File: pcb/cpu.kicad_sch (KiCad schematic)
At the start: 12 parts, among them J9 x2 Multiplier, U1 486Socket

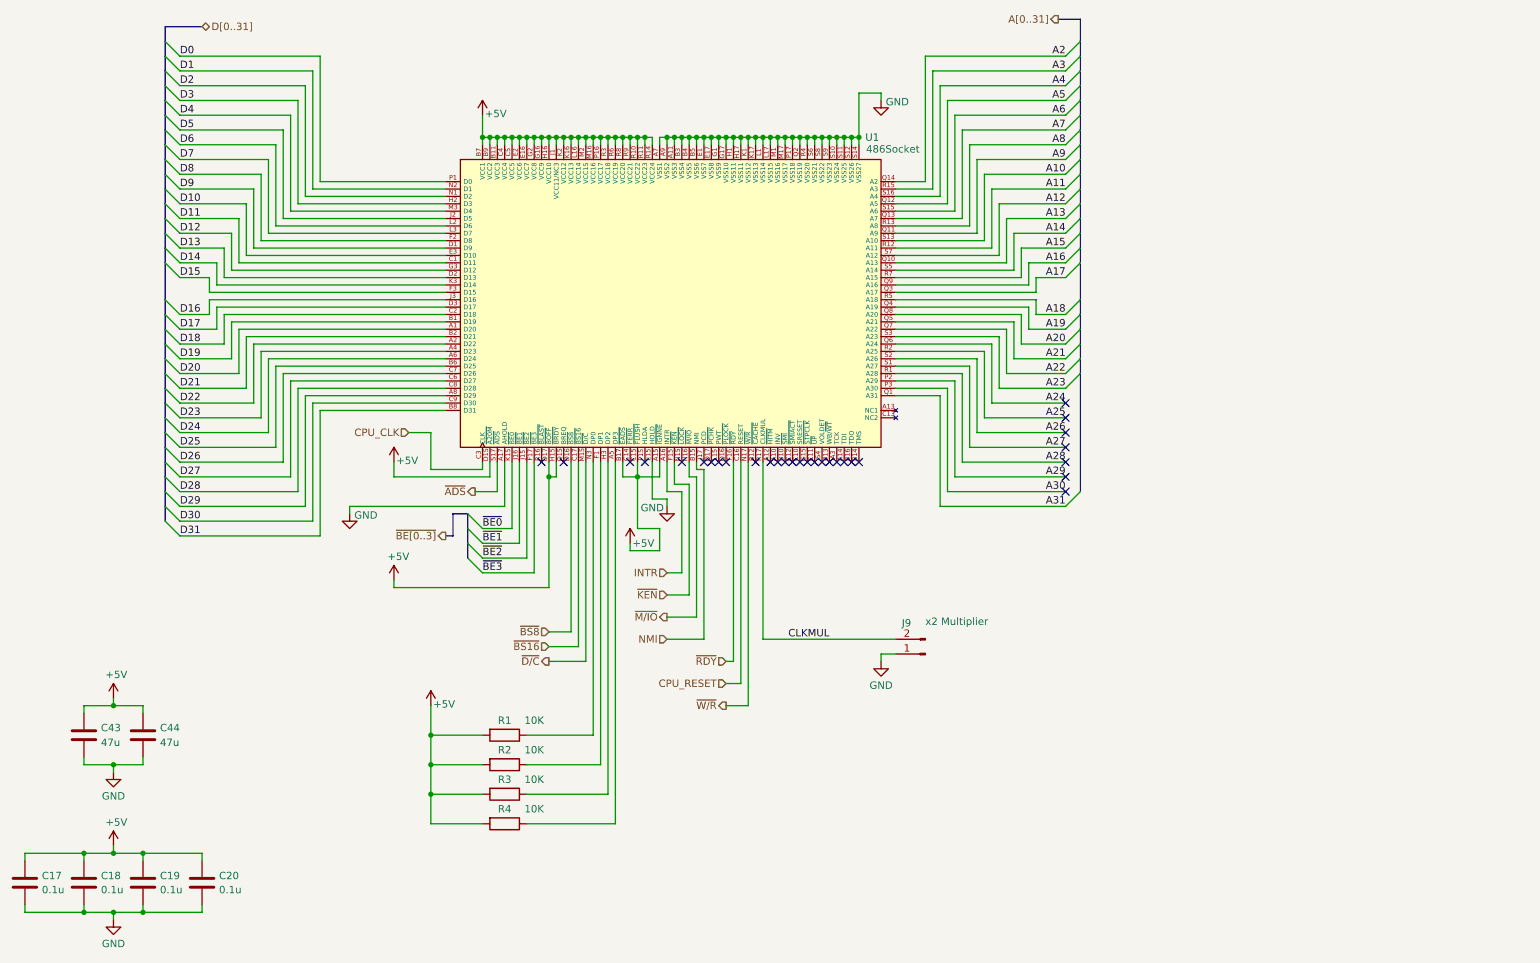
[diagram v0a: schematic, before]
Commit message: CPU diagram DMA/Burst pins pulled out to test points near FPGA IO ready for experimentation
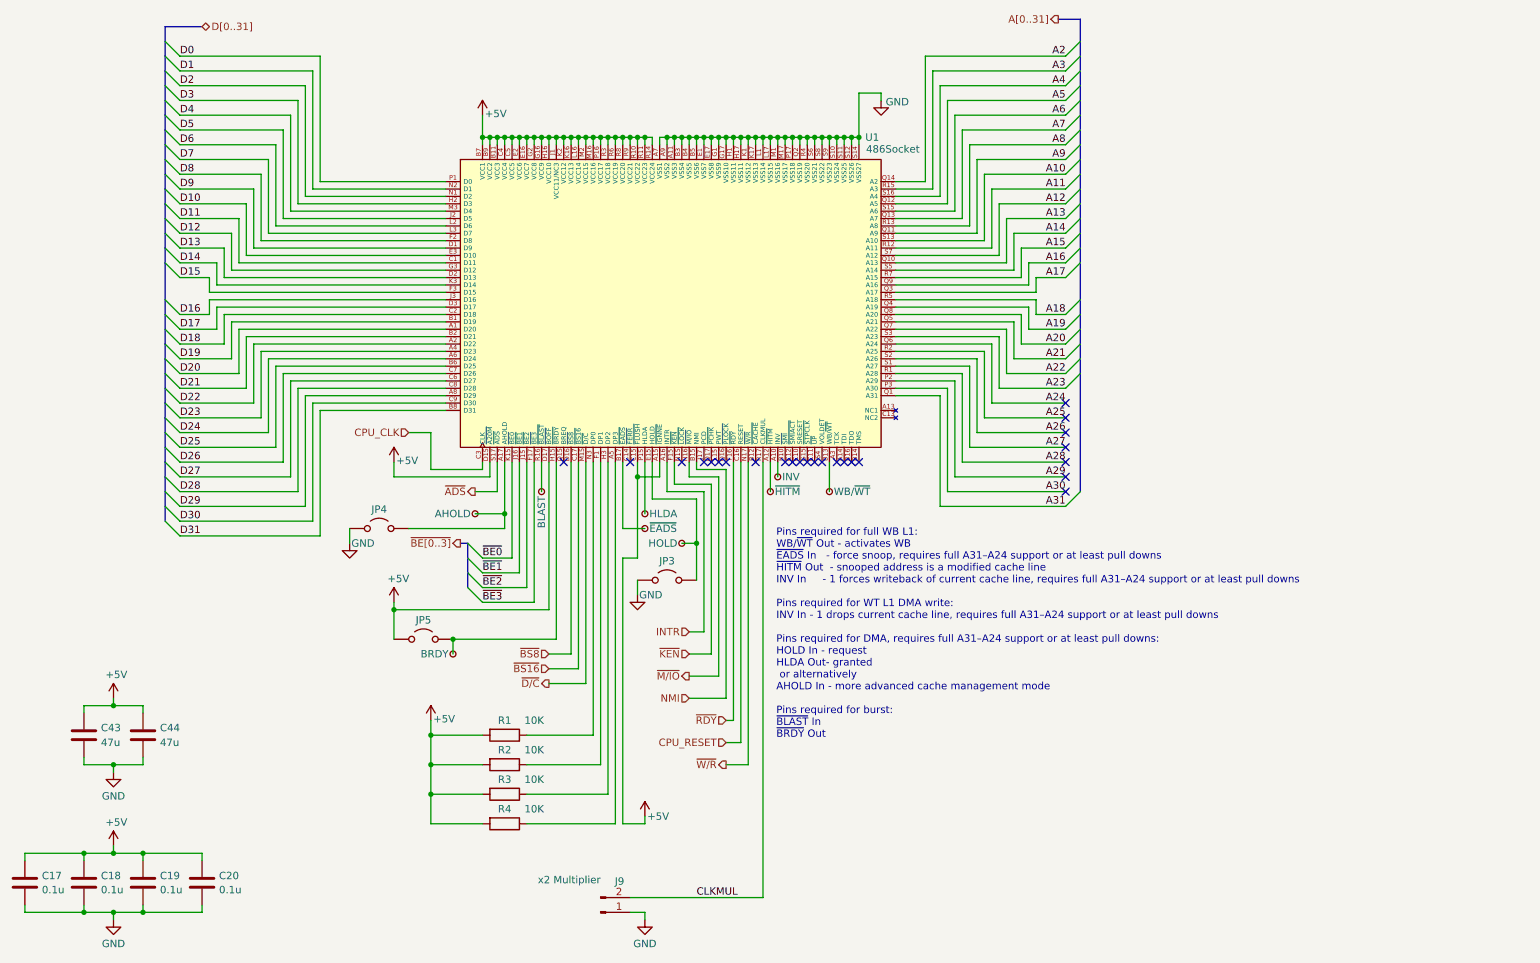
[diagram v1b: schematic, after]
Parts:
- added JP3, JP4, JP5: Jumper_2_Open, Jumper:SolderJumper-2_P1.3mm_Open_TrianglePad1.0x1.5mm, symbol Jumper:Jumper_2_Open
- added TP10: INV, 486custom:TestPoint_Pad_D0.4mm, symbol Connector:TestPoint_Small
- added TP11: ~{EADS}, 486custom:TestPoint_Pad_D0.4mm, symbol Connector:TestPoint_Small
- added TP12: AHOLD, 486custom:TestPoint_Pad_D0.4mm, symbol Connector:TestPoint_Small
- added TP13: BLAST, 486custom:TestPoint_Pad_D0.4mm, symbol Connector:TestPoint_Small
- added TP14: BRDY, 486custom:TestPoint_Pad_D0.4mm, symbol Connector:TestPoint_Small
- added TP6: WB/~{WT}, 486custom:TestPoint_Pad_D0.4mm, symbol Connector:TestPoint_Small
- added TP7: ~{HITM}, 486custom:TestPoint_Pad_D0.4mm, symbol Connector:TestPoint_Small
- added TP8: HLDA, 486custom:TestPoint_Pad_D0.4mm, symbol Connector:TestPoint_Small
- added TP9: HOLD, 486custom:TestPoint_Pad_D0.4mm, symbol Connector:TestPoint_Small
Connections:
- net +5V: now also JP5.1 (A); no longer U1.B17 (~{EADS}), U1.H15 (~{BRDY})
- net GND: now also JP3.1 (A), JP4.1 (A); no longer U1.A17 (AHOLD), U1.E15 (HOLD)
- net at U1.A10 (INV): now also TP10.1
- net at U1.A12 (~{HITM}): now also TP7.1
- net at U1.B13 (WB/~{WT}): now also TP6.1
- net at U1.P15 (HLDA): now also TP8.1
- net at U1.R16 (~{BLAST}): now also TP13.1
- new net: JP5.2 (B), TP14.1, U1.H15 (~{BRDY})
- new net: JP4.2 (B), TP12.1, U1.A17 (AHOLD)
- new net: TP11.1, U1.B17 (~{EADS})
- new net: JP3.2 (B), TP9.1, U1.E15 (HOLD)
- no-connect marks 30 -> 25
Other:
- note added: "Pins required for full WB L1: WB/~{WT} Out - activates WB ~{EADS} In - force snoop, requires full A31–A24 support or at least pull downs ~{HITM} Out - snooped address is a modified cache line INV In - 1 forces writeback of current cache line, requires full A31–A24 support or at least pull downs Pins required for WT L1 DMA write: INV In - 1 drops current cache line, requires full A31–A24 support o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"
- moved on the sheet: J9

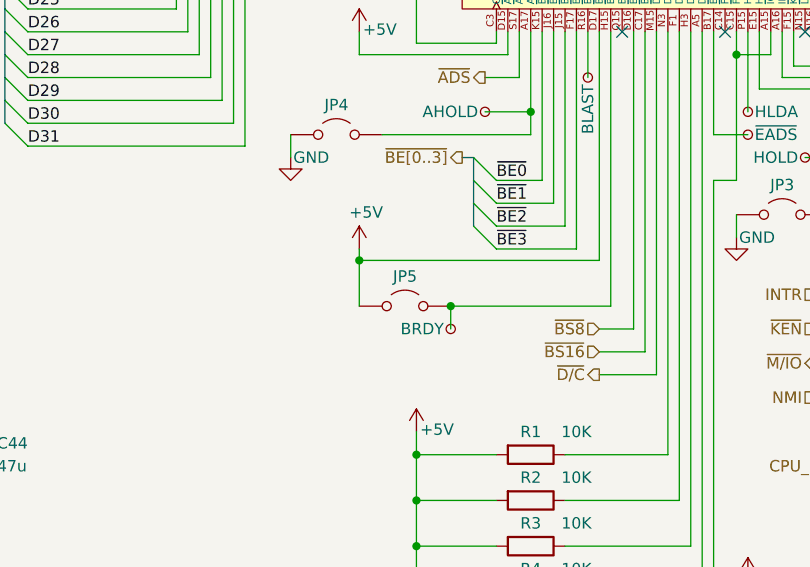
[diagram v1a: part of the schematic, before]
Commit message: BRDY has internal pullup, no external needed
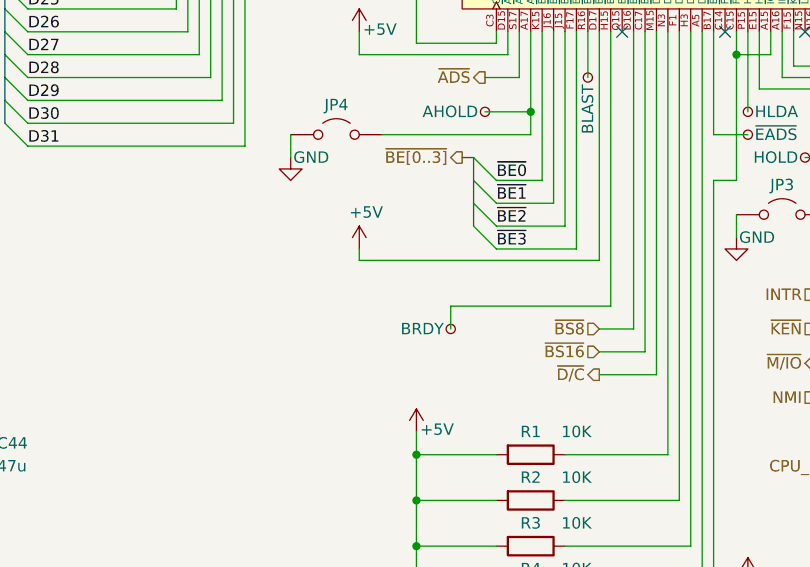
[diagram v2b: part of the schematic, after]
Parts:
- removed JP5: Jumper_2_Open, Jumper:SolderJumper-2_P1.3mm_Open_TrianglePad1.0x1.5mm, symbol Jumper:Jumper_2_Open
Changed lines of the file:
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@@
 	)
 	(junction
-		(at 114.3 135.89)
-		(diameter 0)
-		(color 0 0 0 0)
-	)
-	(junction
 		(at 162.56 49.53)
 		(diameter 0)
@@
 	)
 	(junction
-		(at 104.14 130.81)
-		(diameter 0)
-		(color 0 0 0 0)
-	)
-	(junction
 		(at 158.75 49.53)
 		(diameter 0)
@@
 	(wire
 		(pts
-			(xy 104.14 130.81) (xy 104.14 135.89)
-		)
-		(stroke
-			(width 0)
-			(type default)
-		)
-	)
-	(wire
-		(pts
 			(xy 129.54 110.49) (xy 129.54 105.41)
 		)
@@
 					(unit 1)
 				)
-			)
-		)
-	)
-	(symbol
-		(lib_id "Jumper:Jumper_2_Open")
-		(at 109.22 135.89 0)
-		(unit 1)
-		(exclude_from_sim no)
-		(in_bom yes)
-		(on_board yes)
-		(dnp no)
-		(property "Reference" "JP5"
-			(at 109.22 132.588 0)
-			(effects
-				(font
-					(size 1.27 1.27)
-				)
-			)
-		)
-		(property "Value" "Jumper_2_Open"
-			(at 109.22 132.08 0)
-			(effects
-				(font
-					(size 1.27 1.27)
-				)
-				(hide yes)
-			)
-		)
-		(property "Footprint" "Jumper:SolderJumper-2_P1.3mm_Open_TrianglePad1.0x1.5mm"
-			(at 109.22 135.89 0)
-			(effects
-				(font
-					(size 1.27 1.27)
-				)
-				(hide yes)
-			)
-		)
-		(property "Datasheet" "~"
-			(at 109.22 135.89 0)
-			(effects
-				(font
-					(size 1.27 1.27)
-				)
-				(hide yes)
-			)
-		)
-		(property "Description" "Jumper, 2-pole, open"
-			(at 109.22 135.89 0)
-			(effects
-				(font
-					(size 1.27 1.27)
-				)
-				(hide yes)
-			)
-		)
-		(pin "2"
-		)
-		(pin "1"
-		)
-		(instances
-			(project "homebrew_486"
-				(path "/360fb3b9-a21a-4226-8954-bf45cf17bb35/98e7b245-1892-4961-80dc-a2961de8ec76"
-					(reference "JP5")
-					(unit 1)
-				)

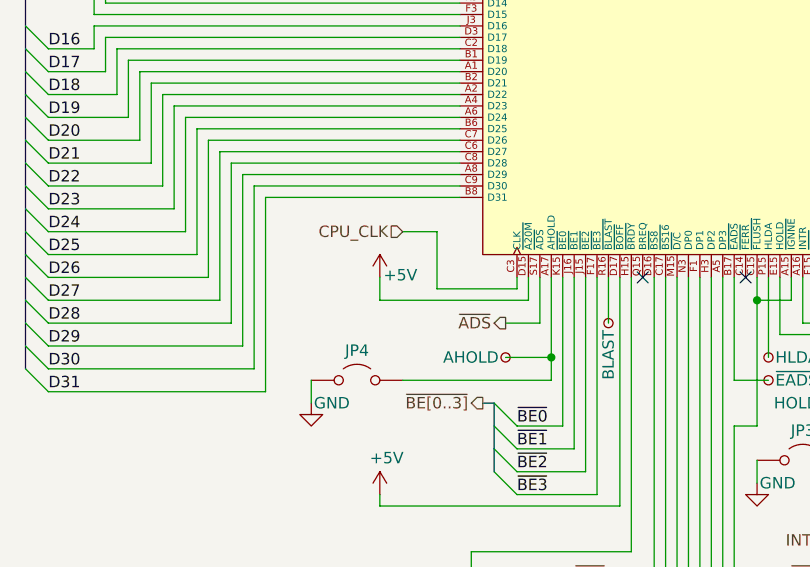
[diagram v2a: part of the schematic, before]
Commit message: CPU pulled A20M nar the AVR and made pullup optional. Enables control of A20M by AVR like old school Keyboard controllers did in 286.
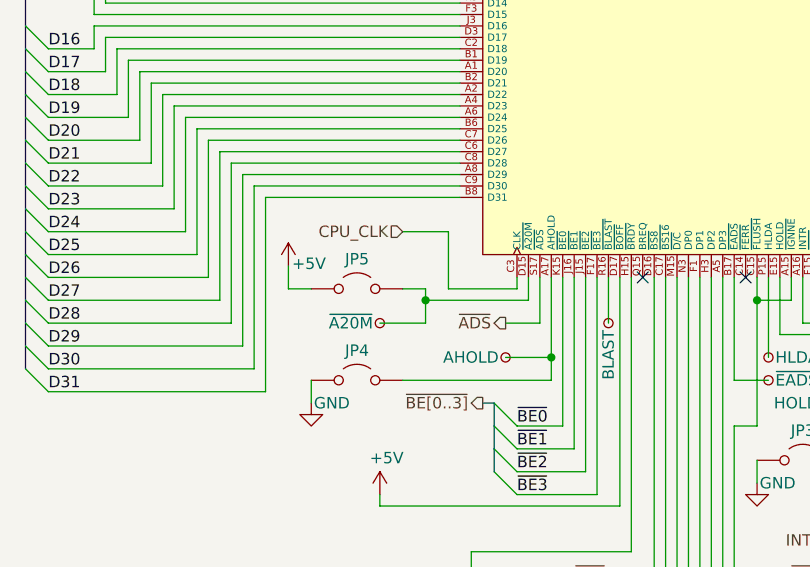
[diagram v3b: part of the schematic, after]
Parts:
- added JP5: Jumper_2_Open, Jumper:SolderJumper-2_P1.3mm_Open_TrianglePad1.0x1.5mm, symbol Jumper:Jumper_2_Open
- added TP15: ~{A20M}, 486custom:TestPoint_Pad_D0.4mm, symbol Connector:TestPoint_Small
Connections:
- net +5V: now also JP5.1 (A); no longer U1.D15 (~{A20M})
- new net: JP5.2 (B), TP15.1, U1.D15 (~{A20M})
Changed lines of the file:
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@@
 	)
 	(junction
+		(at 109.22 107.95)
+		(diameter 0)
+		(color 0 0 0 0)
+	)
+	(junction
 		(at 181.61 49.53)
 		(diameter 0)
@@
 	(wire
 		(pts
+			(xy 109.22 107.95) (xy 109.22 110.49)
+		)
+		(stroke
+			(width 0)
+			(type default)
+		)
+	)
+	(wire
+		(pts
 			(xy 142.24 49.53) (xy 140.97 49.53)
 		)
@@
 	(wire
 		(pts
-			(xy 110.49 106.68) (xy 119.38 106.68)
+			(xy 111.76 106.68) (xy 119.38 106.68)
 		)
 		(stroke
@@
 	(wire
 		(pts
+			(xy 93.98 106.68) (xy 93.98 104.14)
+		)
+		(stroke
+			(width 0)
+			(type default)
+		)
+	)
+	(wire
+		(pts
 			(xy 88.9 59.69) (xy 113.03 59.69)
 		)
@@
 	(wire
 		(pts
-			(xy 106.68 100.33) (xy 110.49 100.33)
+			(xy 106.68 100.33) (xy 111.76 100.33)
 		)
 		(stroke
@@
 	(wire
 		(pts
-			(xy 110.49 100.33) (xy 110.49 106.68)
+			(xy 111.76 100.33) (xy 111.76 106.68)
 		)
 		(stroke
@@
 	(wire
 		(pts
+			(xy 109.22 106.68) (xy 109.22 107.95)
+		)
+		(stroke
+			(width 0)
+			(type default)
+		)
+	)
+	(wire
+		(pts
 			(xy 205.74 86.36) (xy 205.74 97.79)
 		)
@@
 	(wire
 		(pts
+			(xy 109.22 107.95) (xy 120.65 107.95)
+		)
+		(stroke
+			(width 0)
+			(type default)
+		)
+	)
+	(wire
+		(pts
 			(xy 165.1 49.53) (xy 163.83 49.53)
 		)
@@
 	(wire
 		(pts
+			(xy 104.14 110.49) (xy 109.22 110.49)
+		)
+		(stroke
+			(width 0)
+			(type default)
+		)
+	)
+	(wire
+		(pts
 			(xy 90.17 95.25) (xy 113.03 95.25)
 		)
@@
 	(wire
 		(pts
+			(xy 96.52 106.68) (xy 93.98 106.68)
+		)
+		(stroke
+			(width 0)
+			(type default)
+		)
+	)
+	(wire
+		(pts
 			(xy 96.52 119.38) (xy 96.52 116.84)
 		)
@@
 	(wire
 		(pts
+			(xy 109.22 106.68) (xy 106.68 106.68)
+		)
+		(stroke
+			(width 0)
+			(type default)
+		)
+	)
+	(wire
+		(pts
 			(xy 50.8 172.72) (xy 50.8 173.99)
 		)
@@
 	(wire
 		(pts
-			(xy 104.14 107.95) (xy 104.14 105.41)
-		)
-		(stroke
-			(width 0)
-			(type default)
-		)
-	)
-	(wire
-		(pts
 			(xy 91.44 118.11) (xy 91.44 96.52)
 		)
@@
 		)
 	)
-	(wire
-		(pts
-			(xy 104.14 107.95) (xy 120.65 107.95)
-		)
-		(stroke
-			(width 0)
-			(type default)
-		)
-	)
 	(bus
 		(pts
@@
 	)
 	(symbol
+		(lib_id "Connector:TestPoint_Small")
+		(at 104.14 110.49 180)
+		(unit 1)
+		(exclude_from_sim no)
+		(in_bom yes)
+		(on_board yes)
+		(dnp no)
+		(property "Reference" "TP15"
+			(at 110.49 110.49 0)
+			(effects
+				(font
+					(size 1.27 1.27)
+				)
+				(justify left)
+				(hide yes)
+			)
+		)
+		(property "Value" "~{A20M}"
+			(at 103.378 110.49 0)
+			(effects
+				(font
+					(size 1.27 1.27)
+				)
+				(justify left)
+			)
+		)
+		(property "Footprint" "486custom:TestPoint_Pad_D0.4mm"
+			(at 99.06 110.49 0)
+			(effects
+				(font
+					(size 1.27 1.27)
+				)
+				(hide yes)
+			)
+		)
+		(property "Datasheet" "~"
+			(at 99.06 110.49 0)
+			(effects
+				(font
+					(size 1.27 1.27)
+				)
+				(hide yes)
+			)
+		)
+		(property "Description" "test point"
+			(at 104.14 110.49 0)
+			(effects
+				(font
+					(size 1.27 1.27)
+				)
+				(hide yes)
+			)
+		)
+		(pin "1"
+		)
+		(instances
+			(project "homebrew_486"
+				(path "/360fb3b9-a21a-4226-8954-bf45cf17bb35/98e7b245-1892-4961-80dc-a2961de8ec76"
+					(reference "TP15")
+					(unit 1)
+				)
+			)
+		)
+	)
+	(symbol
 		(lib_id "power:GND")
 		(at 55.88 158.75 0)
@@
 	(symbol
 		(lib_id "power:+5V")
-		(at 104.14 105.41 0)
+		(at 93.98 104.14 0)
 		(unit 1)
 		(exclude_from_sim no)
@@
 		(dnp no)
 		(property "Reference" "#PWR03"
-			(at 104.14 109.22 0)
+			(at 93.98 107.95 0)
 			(effects
 				(font
@@
 		)
 		(property "Value" "+5V"
-			(at 106.426 105.156 0)
+			(at 96.266 103.886 0)
 			(effects
 				(font
@@
 		)
 		(property "Footprint" ""
-			(at 104.14 105.41 0)
+			(at 93.98 104.14 0)
 			(effects
 				(font
@@
 		)
 		(property "Datasheet" ""
-			(at 104.14 105.41 0)
+			(at 93.98 104.14 0)
 			(effects
 				(font
@@
 		)
 		(property "Description" "Power symbol creates a global label with name \"+5V\""
-			(at 104.14 105.41 0)
+			(at 93.98 104.14 0)
 			(effects
 				(font
@@
 					(unit 1)
 				)
+			)
+		)
+	)
+	(symbol
+		(lib_id "Jumper:Jumper_2_Open")
+		(at 101.6 106.68 0)
+		(unit 1)
+		(exclude_from_sim no)
+		(in_bom yes)
+		(on_board yes)
+		(dnp no)
+		(property "Reference" "JP5"
+			(at 101.6 103.378 0)
+			(effects
+				(font
+					(size 1.27 1.27)
+				)
+			)
+		)
+		(property "Value" "Jumper_2_Open"
+			(at 101.6 102.87 0)
+			(effects
+				(font
+					(size 1.27 1.27)
+				)
+				(hide yes)
+			)
+		)
+		(property "Footprint" "Jumper:SolderJumper-2_P1.3mm_Open_TrianglePad1.0x1.5mm"
+			(at 101.6 106.68 0)
+			(effects
+				(font
+					(size 1.27 1.27)
+				)
+				(hide yes)
+			)
+		)
+		(property "Datasheet" "~"
+			(at 101.6 106.68 0)
+			(effects
+				(font
+					(size 1.27 1.27)
+				)
+				(hide yes)
+			)
+		)
+		(property "Description" "Jumper, 2-pole, open"
+			(at 101.6 106.68 0)
+			(effects
+				(font
+					(size 1.27 1.27)
+				)
+				(hide yes)
+			)
+		)
+		(pin "2"
+		)
+		(pin "1"
+		)
+		(instances
+			(project "homebrew_486"
+				(path "/360fb3b9-a21a-4226-8954-bf45cf17bb35/98e7b245-1892-4961-80dc-a2961de8ec76"
+					(reference "JP5")
+					(unit 1)
+				)
